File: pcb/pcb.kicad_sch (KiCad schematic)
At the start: 27 parts, among them J1 Screw_Terminal_01x02, J2 Screw_Terminal_01x04, J3 Screw_Terminal_01x04, J5 Screw_Terminal_01x06, J6 Screw_Terminal_01x04, Q1 2N7000, Q2 2N7000, Q3 2N7000

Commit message: finished layout
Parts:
- added ExtraTerminalBlock1: Screw_Terminal_01x04, TerminalBlock:TerminalBlock_MaiXu_MX126-5.0-04P_1x04_P5.00mm, symbol Connector:Screw_Terminal_01x04
- renumbered R2 to mix1, R3 to mix2, R4 to mix3, InputCap2 to motor_c1, InputCap1 to reg_ci1, OutputCap1 to reg_co1, OutputCap2 to vd_c1, OutputCap3 to vd_c2, R1 to vd_r1
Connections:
- net at ESP32-S3.1 (3V3), J6.4 (Pin_4), MovingBumper_back1.2 (Pin_2)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: now also ExtraTerminalBlock1.4 (Pin_4)
- net at ESP32-S3.40 (21): now also ExtraTerminalBlock1.1 (Pin_1)
- net at ESP32-S3.41 (20): now also ExtraTerminalBlock1.2 (Pin_2)
- net at ESP32-S3.44 (GND): now also ExtraTerminalBlock1.3 (Pin_3)

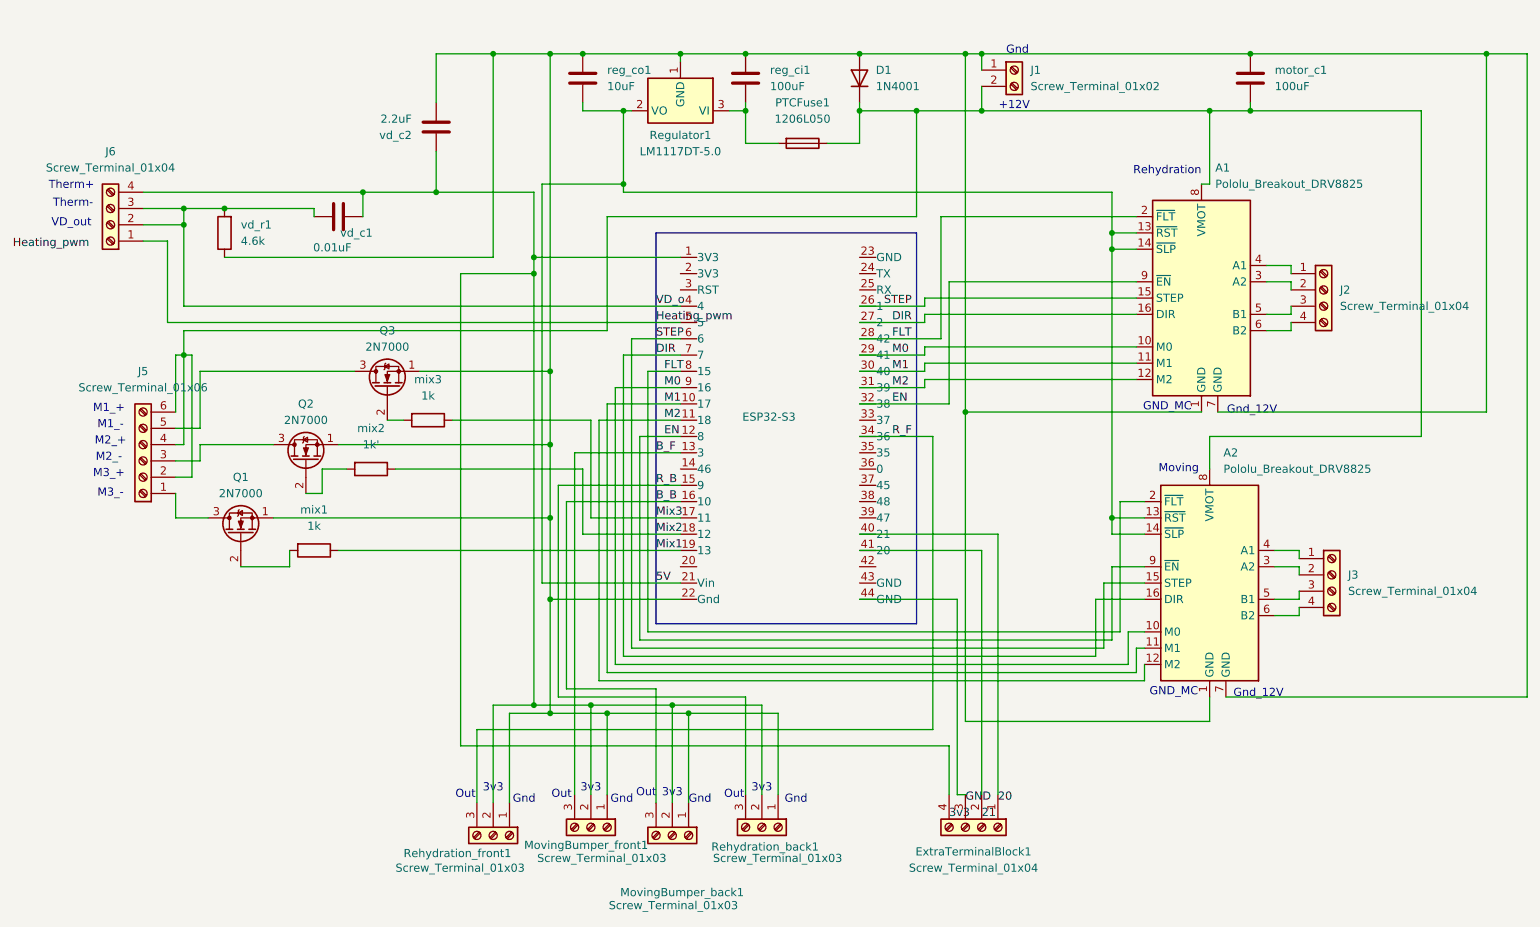
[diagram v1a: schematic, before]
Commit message: edit names of blocks
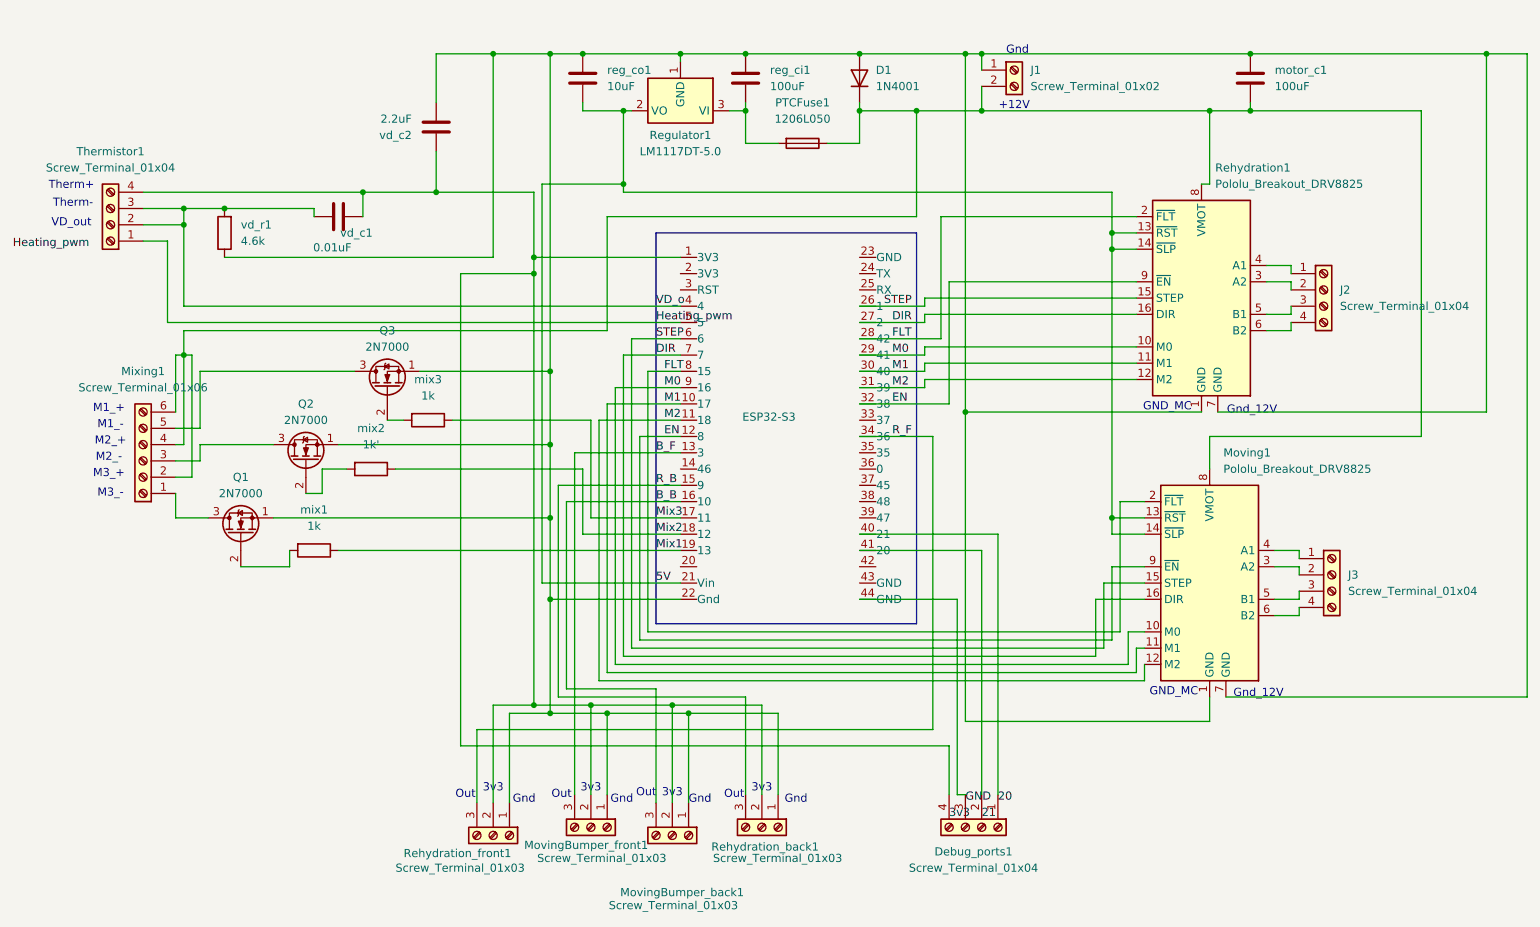
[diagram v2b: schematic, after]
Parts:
- renumbered ExtraTerminalBlock1 to Debug_ports1, J5 to Mixing1, A2 to Moving1, A1 to Rehydration1, J6 to Thermistor1
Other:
- note removed: "Moving"
- note removed: "Rehydration"
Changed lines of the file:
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@@
 		)
 	)
-	(text "Rehydration\n"
-		(exclude_from_sim no)
-		(at 220.726 42.418 0)
-		(effects
-			(font
-				(size 1.27 1.27)
-			)
-		)
-	)
 	(text "3v3"
 		(exclude_from_sim no)
@@
 		)
 	)
-	(text "Moving\n"
-		(exclude_from_sim no)
-		(at 222.504 88.9 0)
-		(effects
-			(font
-				(size 1.27 1.27)
-			)
-		)
-	)
 	(text "M2_+"
 		(exclude_from_sim no)
@@
 		(dnp no)
 		(fields_autoplaced yes)
-		(property "Reference" "J6"
+		(property "Reference" "Thermistor1"
 			(at 55.88 39.37 0)
 			(effects
@@
 			(project ""
 				(path "/5b8f4b4b-fd94-4673-8b66-f0a593fc8259"
-					(reference "J6")
+					(reference "Thermistor1")
 					(unit 1)
 				)
@@
 		(dnp no)
 		(fields_autoplaced yes)
-		(property "Reference" "A2"
+		(property "Reference" "Moving1"
 			(at 229.4733 86.36 0)
 			(effects
@@
 			(project "pcb"
 				(path "/5b8f4b4b-fd94-4673-8b66-f0a593fc8259"
-					(reference "A2")
+					(reference "Moving1")
 					(unit 1)
 				)
@@
 		(dnp no)
 		(fields_autoplaced yes)
-		(property "Reference" "A1"
+		(property "Reference" "Rehydration1"
 			(at 228.2033 41.91 0)
 			(effects
@@
 			(project ""
 				(path "/5b8f4b4b-fd94-4673-8b66-f0a593fc8259"
-					(reference "A1")
+					(reference "Rehydration1")
 					(unit 1)
 				)
@@
 		(dnp no)
 		(fields_autoplaced yes)
-		(property "Reference" "ExtraTerminalBlock1"
+		(property "Reference" "Debug_ports1"
 			(at 190.5 148.59 90)
 			(effects
@@
 			(project ""
 				(path "/5b8f4b4b-fd94-4673-8b66-f0a593fc8259"
-					(reference "ExtraTerminalBlock1")
+					(reference "Debug_ports1")
 					(unit 1)
 				)
@@
 		(dnp no)
 		(fields_autoplaced yes)
-		(property "Reference" "J5"
+		(property "Reference" "Mixing1"
 			(at 60.96 73.66 0)
 			(effects
@@
 			(project ""
 				(path "/5b8f4b4b-fd94-4673-8b66-f0a593fc8259"
-					(reference "J5")
+					(reference "Mixing1")
 					(unit 1)
 				)

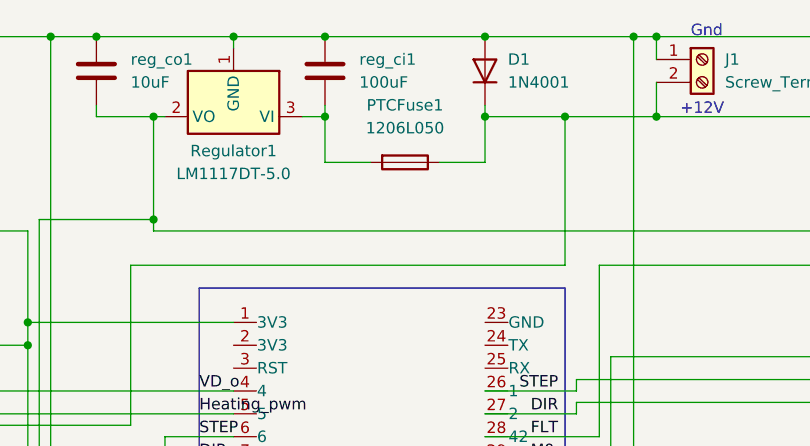
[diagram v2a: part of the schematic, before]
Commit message: forgot to pull, gonna force push this. I changed everything to through holes so we can soulder easier, added the board info onto pcb
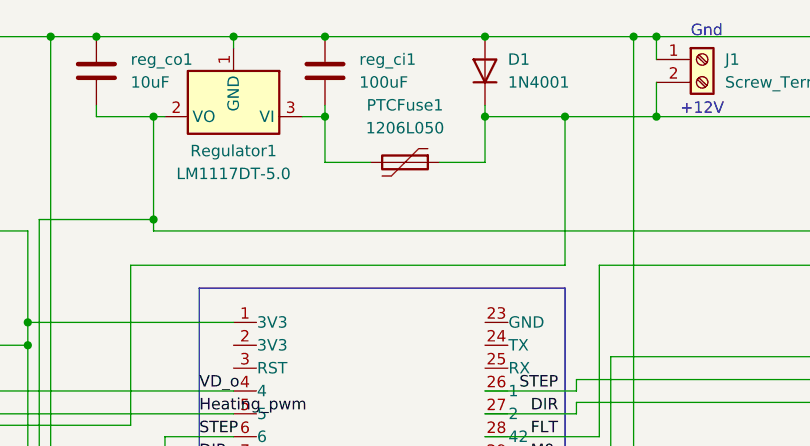
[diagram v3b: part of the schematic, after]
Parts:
- PTCFuse1: footprint Resistor_SMD:R_1206_3216Metric -> Fuse:Fuse_1206_3216Metric_Pad1.42x1.75mm_HandSolder; symbol Device:Fuse -> Device:Polyfuse
- mix1, mix2, mix3, vd_r1: footprint Resistor_SMD:R_0805_2012Metric -> Resistor_THT:R_Axial_DIN0207_L6.3mm_D2.5mm_P7.62mm_Horizontal
- motor_c1, reg_ci1: footprint Capacitor_SMD:C_0805_2012Metric -> Capacitor_THT:CP_Radial_D6.3mm_P2.50mm
- reg_co1, vd_c2: footprint Capacitor_SMD:C_0805_2012Metric -> Capacitor_THT:CP_Radial_D5.0mm_P2.50mm
- vd_c1: footprint Capacitor_SMD:C_0805_2012Metric -> Capacitor_THT:C_Disc_D3.0mm_W1.6mm_P2.50mm
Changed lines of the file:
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@@
 			)
 		)
-		(property "Footprint" "Resistor_SMD:R_0805_2012Metric"
+		(property "Footprint" "Resistor_THT:R_Axial_DIN0207_L6.3mm_D2.5mm_P7.62mm_Horizontal"
 			(at 87.63 99.822 90)
 			(effects
@@
 			)
 		)
-		(property "Footprint" "Resistor_SMD:R_0805_2012Metric"
+		(property "Footprint" "Resistor_THT:R_Axial_DIN0207_L6.3mm_D2.5mm_P7.62mm_Horizontal"
 			(at 96.52 87.122 90)
 			(effects
@@
 	)
 	(symbol
-		(lib_id "Device:Fuse")
+		(lib_id "Device:Polyfuse")
 		(at 163.83 38.1 270)
 		(unit 1)
@@
 			)
 		)
-		(property "Footprint" "Resistor_SMD:R_1206_3216Metric"
-			(at 163.83 36.322 90)
-			(effects
-				(font
-					(size 1.27 1.27)
-				)
+		(property "Footprint" "Fuse:Fuse_1206_3216Metric_Pad1.42x1.75mm_HandSolder"
+			(at 158.75 39.37 0)
+			(effects
+				(font
+					(size 1.27 1.27)
+				)
+				(justify left)
 				(hide yes)
 			)
@@
 			)
 		)
-		(property "Description" "Fuse"
+		(property "Description" "Resettable fuse, polymeric positive temperature coefficient"
 			(at 163.83 38.1 0)
 			(effects
@@
 			)
 		)
-		(property "Footprint" "Capacitor_SMD:C_0805_2012Metric"
+		(property "Footprint" "Capacitor_THT:CP_Radial_D5.0mm_P2.50mm"
 			(at 130.5052 31.75 0)
 			(effects
@@
 			)
 		)
-		(property "Footprint" "Resistor_SMD:R_0805_2012Metric"
+		(property "Footprint" "Resistor_THT:R_Axial_DIN0207_L6.3mm_D2.5mm_P7.62mm_Horizontal"
 			(at 75.438 52.07 90)
 			(effects
@@
 			)
 		)
-		(property "Footprint" "Capacitor_SMD:C_0805_2012Metric"
+		(property "Footprint" "Capacitor_THT:CP_Radial_D6.3mm_P2.50mm"
 			(at 155.9052 31.75 0)
 			(effects
@@
 			)
 		)
-		(property "Footprint" "Resistor_SMD:R_0805_2012Metric"
+		(property "Footprint" "Resistor_THT:R_Axial_DIN0207_L6.3mm_D2.5mm_P7.62mm_Horizontal"
 			(at 105.41 79.502 90)
 			(effects
@@
 			)
 		)
-		(property "Footprint" "Capacitor_SMD:C_0805_2012Metric"
+		(property "Footprint" "Capacitor_THT:CP_Radial_D6.3mm_P2.50mm"
 			(at 234.6452 31.75 0)
 			(effects
@@
 			)
 		)
-		(property "Footprint" "Capacitor_SMD:C_0805_2012Metric"
+		(property "Footprint" "Capacitor_THT:C_Disc_D3.0mm_W1.6mm_P2.50mm"
 			(at 95.25 48.5648 0)
 			(effects
@@
 			)
 		)
-		(property "Footprint" "Capacitor_SMD:C_0805_2012Metric"
+		(property "Footprint" "Capacitor_THT:CP_Radial_D5.0mm_P2.50mm"
 			(at 105.7148 31.75 0)
 			(effects

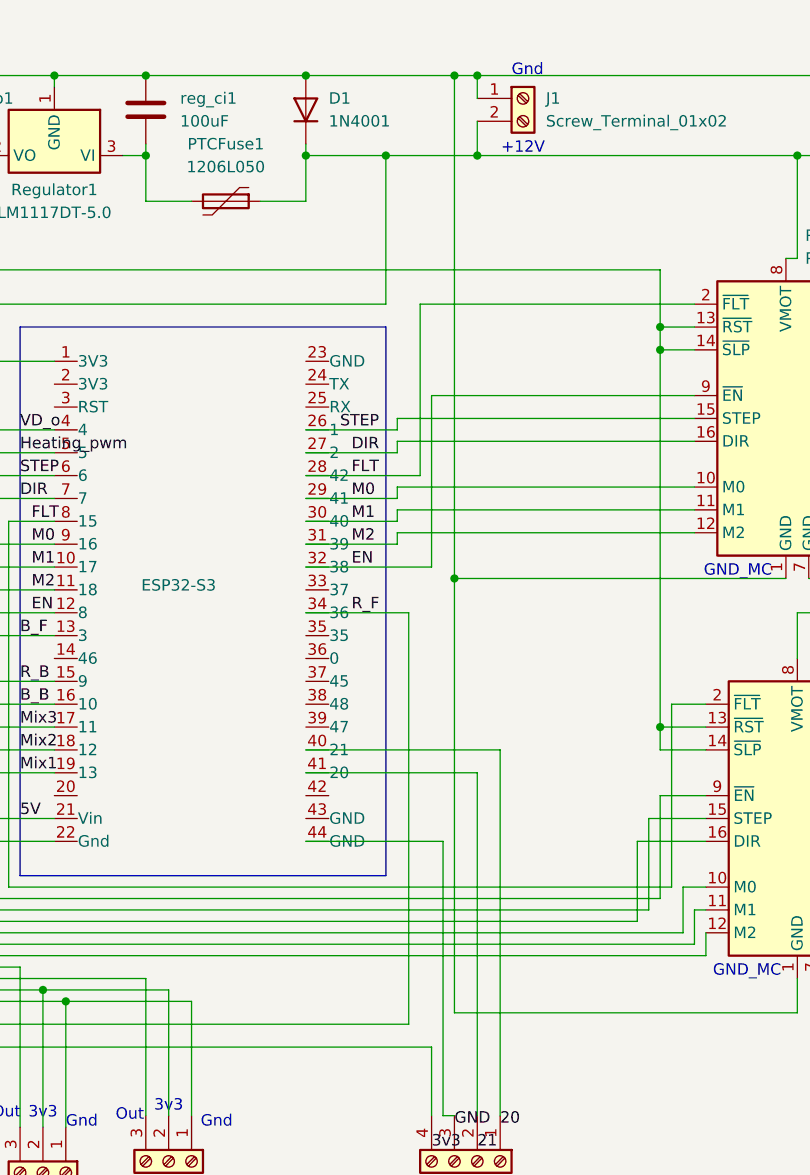
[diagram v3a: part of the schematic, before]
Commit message: edit minimum width, add copper plate
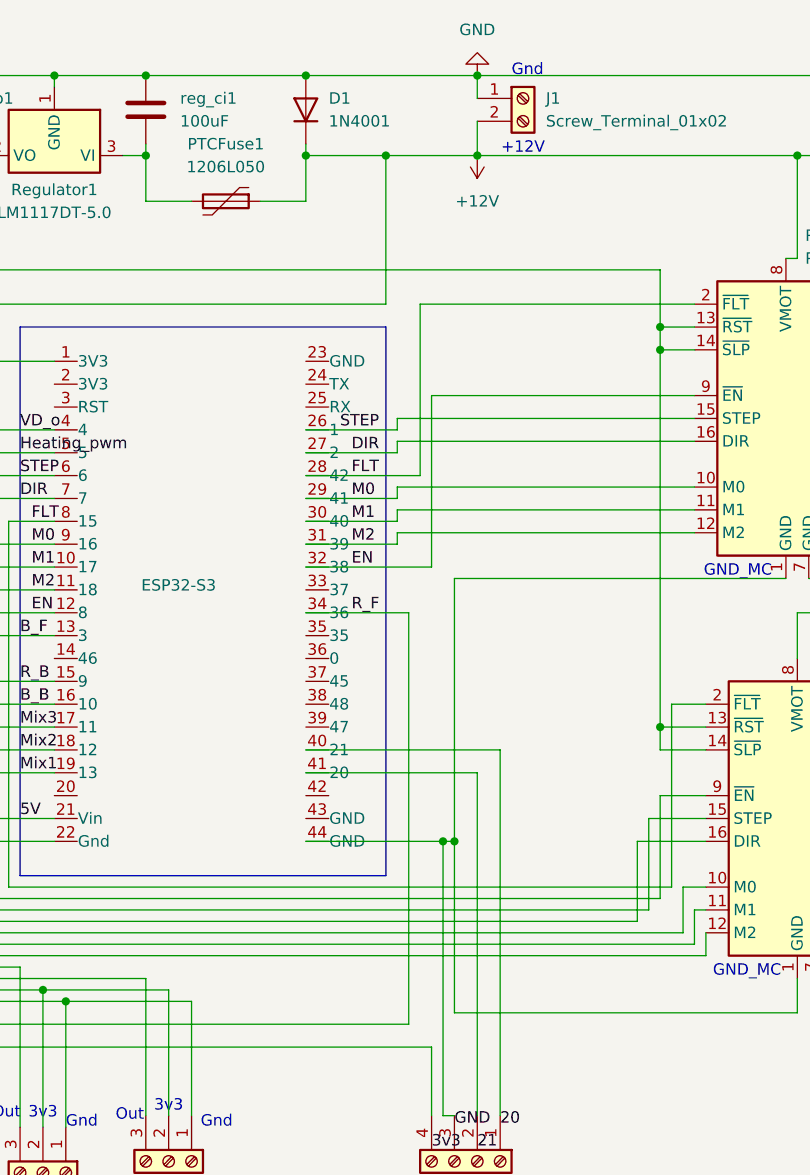
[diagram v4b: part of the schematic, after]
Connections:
- net GND: now also D1.2 (A), ESP32-S3.22 (Gnd), J1.1 (Pin_1), Moving1.7 (GND), MovingBumper_back1.1 (Pin_1), MovingBumper_front1.1 (Pin_1), Q1.1 (S), Q2.1 (S), Q3.1 (S), Regulator1.1 (GND), Rehydration1.7 (GND), Rehydration_back1.1 (Pin_1), Rehydration_front1.1 (Pin_1), motor_c1.1, reg_ci1.1, reg_co1.1, vd_c2.2, vd_r1.1
- net at Debug_ports1.3 (Pin_3), ESP32-S3.44 (GND): now also Moving1.1 (GND), Rehydration1.1 (GND)
- net +12V: now reaches D1.1 (K), J1.2 (Pin_2), Mixing1.2 (Pin_2), Mixing1.4 (Pin_4), Mixing1.6 (Pin_6), Moving1.8 (VMOT), PTCFuse1.1, Rehydration1.8 (VMOT), motor_c1.2
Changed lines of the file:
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@@
 	)
 	(junction
-		(at 189.23 24.13)
-		(diameter 0)
-		(color 0 0 0 0)
-	)
-	(junction
 		(at 73.66 48.26)
 		(diameter 0)
@@
 	)
 	(junction
+		(at 189.23 109.22)
+		(diameter 0)
+		(color 0 0 0 0)
+	)
+	(junction
 		(at 212.09 52.07)
 		(diameter 0)
@@
 	)
 	(junction
+		(at 187.96 109.22)
+		(diameter 0)
+		(color 0 0 0 0)
+	)
+	(junction
 		(at 130.81 125.73)
 		(diameter 0)
@@
 	)
 	(junction
-		(at 189.23 80.01)
-		(diameter 0)
-		(color 0 0 0 0)
-	)
-	(junction
 		(at 106.68 45.72)
 		(diameter 0)
@@
 	(wire
 		(pts
-			(xy 172.72 24.13) (xy 189.23 24.13)
+			(xy 172.72 24.13) (xy 191.77 24.13)
 		)
 		(stroke
@@
 	(wire
 		(pts
-			(xy 189.23 80.01) (xy 189.23 128.27)
+			(xy 189.23 80.01) (xy 189.23 109.22)
 		)
 		(stroke
@@
 	(wire
 		(pts
+			(xy 187.96 109.22) (xy 189.23 109.22)
+		)
+		(stroke
+			(width 0)
+			(type default)
+		)
+	)
+	(wire
+		(pts
 			(xy 124.46 24.13) (xy 124.46 73.66)
 		)
@@
 	(wire
 		(pts
-			(xy 189.23 24.13) (xy 189.23 80.01)
-		)
-		(stroke
-			(width 0)
-			(type default)
-		)
-	)
-	(wire
-		(pts
 			(xy 66.04 92.71) (xy 66.04 96.52)
 		)
@@
 	(wire
 		(pts
-			(xy 189.23 24.13) (xy 191.77 24.13)
-		)
-		(stroke
-			(width 0)
-			(type default)
-		)
-	)
-	(wire
-		(pts
 			(xy 128.27 86.36) (xy 144.78 86.36)
 		)
@@
 	(wire
 		(pts
+			(xy 189.23 109.22) (xy 189.23 128.27)
+		)
+		(stroke
+			(width 0)
+			(type default)
+		)
+	)
+	(wire
+		(pts
 			(xy 73.66 55.88) (xy 115.57 55.88)
 		)
@@
 	)
 	(symbol
+		(lib_id "power:+12V")
+		(at 191.77 33.02 180)
+		(unit 1)
+		(exclude_from_sim no)
+		(in_bom yes)
+		(on_board yes)
+		(dnp no)
+		(fields_autoplaced yes)
+		(property "Reference" "#PWR02"
+			(at 191.77 29.21 0)
+			(effects
+				(font
+					(size 1.27 1.27)
+				)
+				(hide yes)
+			)
+		)
+		(property "Value" "+12V"
+			(at 191.77 38.1 0)
+			(effects
+				(font
+					(size 1.27 1.27)
+				)
+			)
+		)
+		(property "Footprint" ""
+			(at 191.77 33.02 0)
+			(effects
+				(font
+					(size 1.27 1.27)
+				)
+				(hide yes)
+			)
+		)
+		(property "Datasheet" ""
+			(at 191.77 33.02 0)
+			(effects
+				(font
+					(size 1.27 1.27)
+				)
+				(hide yes)
+			)
+		)
+		(property "Description" "Power symbol creates a global label with name \"+12V\""
+			(at 191.77 33.02 0)
+			(effects
+				(font
+					(size 1.27 1.27)
+				)
+				(hide yes)
+			)
+		)
+		(pin "1"
+		)
+		(instances
+			(project ""
+				(path "/5b8f4b4b-fd94-4673-8b66-f0a593fc8259"
+					(reference "#PWR02")
+					(unit 1)
+				)
+			)
+		)
+	)
+	(symbol
 		(lib_id "Driver_Motor:Pololu_Breakout_DRV8825")
 		(at 226.06 59.69 0)
@@
 					(unit 1)
 				)
+			)
+		)
+	)
+	(symbol
+		(lib_id "power:GND")
+		(at 191.77 24.13 180)
+		(unit 1)
+		(exclude_from_sim no)
+		(in_bom yes)
+		(on_board yes)
+		(dnp no)
+		(fields_autoplaced yes)
+		(property "Reference" "#PWR01"
+			(at 191.77 17.78 0)
+			(effects
+				(font
+					(size 1.27 1.27)
+				)
+				(hide yes)
+			)
+		)
+		(property "Value" "GND"
+			(at 191.77 19.05 0)
+			(effects
+				(font
+					(size 1.27 1.27)
+				)
+			)
+		)
+		(property "Footprint" ""
+			(at 191.77 24.13 0)
+			(effects
+				(font
+					(size 1.27 1.27)
+				)
+				(hide yes)
+			)
+		)
+		(property "Datasheet" ""
+			(at 191.77 24.13 0)
+			(effects
+				(font
+					(size 1.27 1.27)
+				)
+				(hide yes)
+			)
+		)
+		(property "Description" "Power symbol creates a global label with name \"GND\" , ground"
+			(at 191.77 24.13 0)
+			(effects
+				(font
+					(size 1.27 1.27)
+				)
+				(hide yes)
+			)
+		)
+		(pin "1"
+		)
+		(instances
+			(project ""
+				(path "/5b8f4b4b-fd94-4673-8b66-f0a593fc8259"
+					(reference "#PWR01")
+					(unit 1)
+				)
